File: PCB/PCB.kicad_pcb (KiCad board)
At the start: 2 copper layers, 51.7 x 66.2 mm, 48 parts, among them IC1 SL2.1A, J1 USB_C_Receptacle_USB2.0_16P, J2 USB_C_Receptacle_USB2.0_16P, J3 USB_C_Receptacle_USB2.0_16P, J4 USB_C_Receptacle_USB2.0_16P, J5 AudioJack4, SW1 Mute_button, U1 PCM2902, U2 USBLC6-2SC6, U3 USBLC6-2SC6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

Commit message: finish pcb and generate gerbers
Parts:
- removed C16: 10uF, Capacitor_SMD:C_0805_2012Metric_Pad1.18x1.45mm_HandSolder
- removed C17: 100nF, Capacitor_SMD:C_0805_2012Metric_Pad1.18x1.45mm_HandSolder
- removed R12: 1k, Resistor_SMD:R_0805_2012Metric_Pad1.20x1.40mm_HandSolder
- C11, C12, C7, C8: footprint Capacitor_SMD:C_0805_2012Metric_Pad1.18x1.45mm_HandSolder -> Capacitor_THT:CP_Radial_D4.0mm_P1.50mm
- moved R16 114.2 mm to (73.5, 87.0)
- moved C8 110.1 mm to (53.8, 91.5), turned to 180 degrees
- moved R10 109.0 mm to (69.2, 97.5), turned to 90 degrees
- moved Y1 109.0 mm to (83.8, 99.0)
- moved R11 108.0 mm to (71.8, 97.5), turned to -90 degrees
- moved C7 102.7 mm to (60.5, 91.6), turned to 180 degrees
- moved R15 95.3 mm to (89.5, 94.2)
- moved C10 89.5 mm to (78.0, 95.8), turned to 180 degrees
- moved C9 86.4 mm to (78.0, 99.0), turned to 180 degrees
- moved C11 85.7 mm to (69.2, 91.0)
- moved C13 85.6 mm to (92.0, 90.2)
- moved C14 85.5 mm to (92.0, 88.2)
- moved C15 85.0 mm to (92.0, 86.2)
- moved U1 84.3 mm to (82.8, 88.1)
- moved R17 84.3 mm to (79.8, 81.1)
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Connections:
- J5 pad S: /Mic -> unconnected-(J5-PadS)
- R10 pad 1: Net-(C17-Pad1) -> GND
- R11 pad 1: Net-(C17-Pad1) -> Net-(U1-VINR)
- R11 pad 2: Net-(U1-VINR) -> GND
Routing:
- net Net-(U1-VOUTR): track 0.00 -> 34.8 mm, vias 0 -> 1
- net +5V: track 147.6 -> 179.6 mm, vias 2 -> 3
- net /Mute: track 11.8 -> 43.4 mm, vias 0 -> 1
- net Net-(U1-VOUTL): track 0.00 -> 26.2 mm, vias 0 -> 1
- net Net-(U1-XTO): track 0.00 -> 24.6 mm, vias 0 -> 2
- net Net-(U1-XTI): track 0.00 -> 24.4 mm, vias 0 -> 1
- net Net-(U1-VINL): track 0.00 -> 16.3 mm
- net Net-(U1-VINR): track 0.00 -> 14.6 mm
- net /D_DAC+: track 12.0 -> 25.6 mm
- net /D_DAC-: track 6.23 -> 18.7 mm
- net Net-(U1-VCCCI): track 4.87 -> 11.5 mm
- net /L_Out: track 0.00 -> 6.26 mm
- net Net-(U1-VBUS): track 0.00 -> 5.52 mm
- net /R_Out: track 0.00 -> 5.21 mm
- net Net-(IC1-XIN): track 10.4 -> 11.1 mm
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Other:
- board size 51.7 x 66.2 mm -> 51.5 x 63 mm

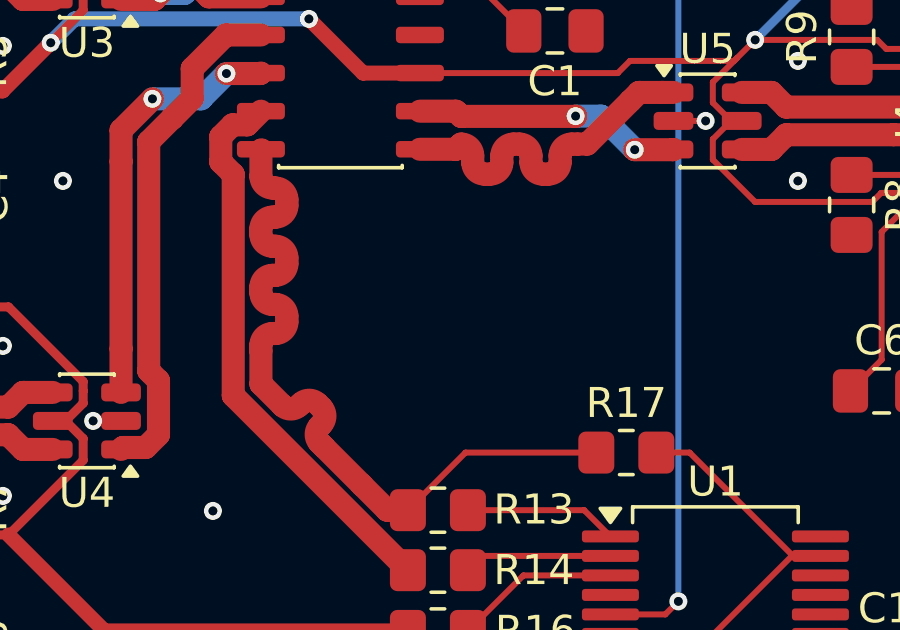
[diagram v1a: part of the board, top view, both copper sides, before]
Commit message: add silkscreen and update gerbers
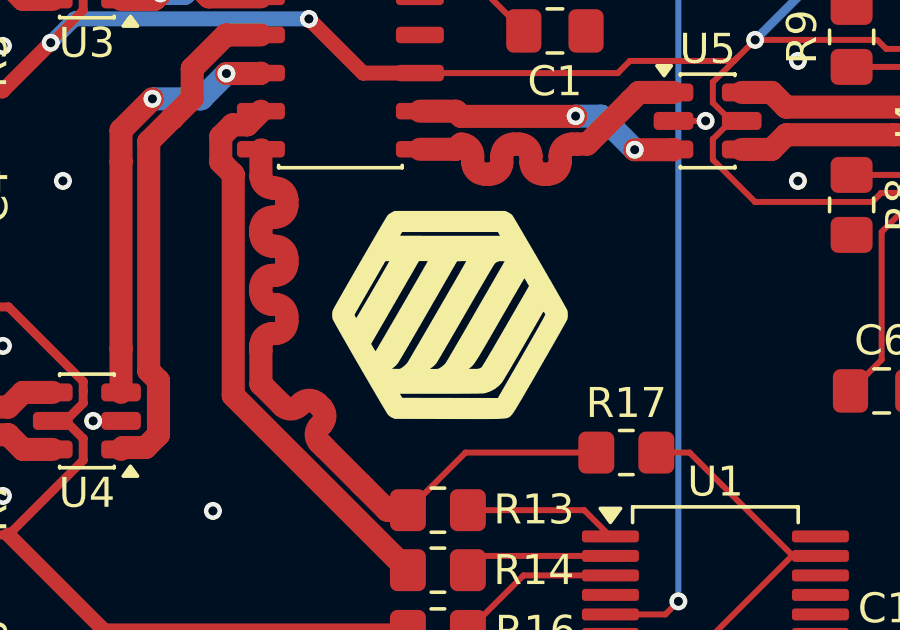
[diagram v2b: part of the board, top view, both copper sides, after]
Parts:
- added G***: LOGO, custom:person20020-logo-8mm, F.Cu at (73.9, 76.5)
